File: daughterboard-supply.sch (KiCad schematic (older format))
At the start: 9 parts

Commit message: Remove power diodes
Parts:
- removed D?: PMEG3005EH, Diode_SMD:D_SOD-123F, symbol Diode:PMEG3005EH
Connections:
- wire segments 25 -> 24
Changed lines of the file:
@@
 VCC12V0
 $Comp
-L Diode:PMEG3005EH D?
-U 1 1 6251677E
-P 2000 1550
-AR Path="/62220F27/6251677E" Ref="D?"  Part="1"
-AR Path="/623923F9/6251677E" Ref="D?"  Part="1"
-F 0 "D?" H 2000 1450 50  0000 C CNN
-F 1 "PMEG3005EH" H 2000 1650 50  0000 C CNN
-F 2 "Diode_SMD:D_SOD-123F" H 2000 1375 50  0001 C CNN
-F 3 "https://assets.nexperia.com/documents/data-sheet/PMEGXX05EH_EJ_SER.pdf" H 2000 1550 50  0001 C CNN
-	1    2000 1550
-	-1   0    0    1
-$EndComp
-$Comp
 L antmicroDCDCConverters:AP62301WU-7 U?
 U 1 1 6251678C
@@
 Connection ~ 2350 1550
 Wire Wire Line
-	1650 1550 1850 1550
-Wire Wire Line
 	5900 1550 5500 1550
 Connection ~ 5500 1550
-Wire Wire Line
-	2150 1550 2350 1550
 $Comp
 L antmicroCapacitors0603:C_10u_16V_0603 C?
@@
 EndData
 $EndBitmap
+Wire Wire Line
+	1650 1550 2350 1550
 $EndSCHEMATC

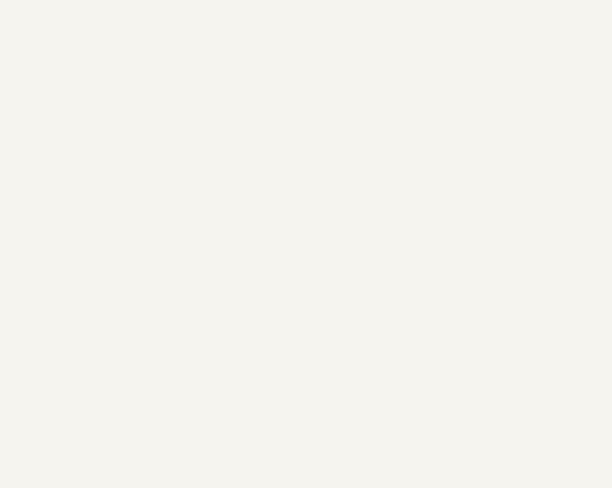
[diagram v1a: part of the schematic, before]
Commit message: Added power distribution connectors
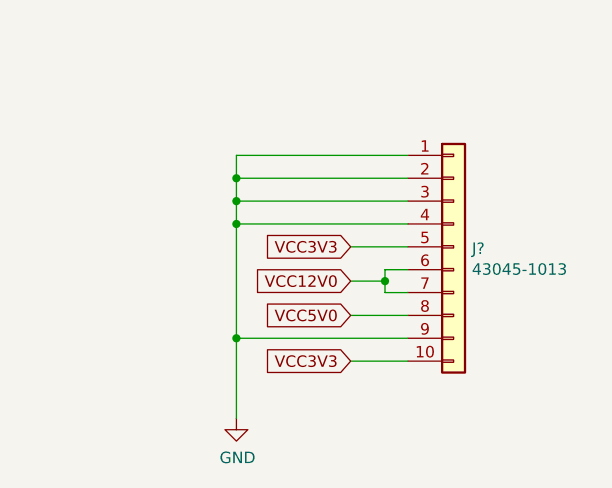
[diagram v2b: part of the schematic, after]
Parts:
- added J?: 43045-1013, antmicro-footprints:43045-1013, symbol antmicroRectangularConnectorsHeadersMalePins:43045-1013
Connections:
- net GND: now also J?.1 (Pin_1), J?.2 (Pin_2), J?.3 (Pin_3), J?.4 (Pin_4), J?.9 (Pin_9)
- net VCC12V0: now also J?.6 (Pin_6), J?.7 (Pin_7)
- net VCC5V0: now also J?.8 (Pin_8)
- new net VCC3V3: J?.10 (Pin_10), J?.5 (Pin_5)
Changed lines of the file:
@@
 Wire Wire Line
 	1650 1550 2350 1550
+$Comp
+L antmicroRectangularConnectorsHeadersMalePins:43045-1013 J?
+U 1 1 62388DA3
+P 9650 1750
+F 0 "J?" H 9730 1792 50  0000 L CNN
+F 1 "43045-1013" H 9730 1701 50  0000 L CNN
+F 2 "antmicro-footprints:43045-1013" H 9650 950 50  0001 C CNN
+F 3 "https://www.molex.com/pdm_docs/sd/430451013_sd.pdf" H 9650 2100 50  0001 C CNN
+F 4 "Molex" H 9650 1050 50  0001 C CNN "Manufacturer"
+F 5 "43045-1013" H 9650 1150 50  0001 C CNN "MPN"
+	1    9650 1750
+	1    0    0    -1
+$EndComp
+$Comp
+L power:GND #PWR?
+U 1 1 62389B5C
+P 8700 2450
+AR Path="/62220F27/62389B5C" Ref="#PWR?"  Part="1"
+AR Path="/623923F9/62389B5C" Ref="#PWR?"  Part="1"
+F 0 "#PWR?" H 8700 2200 50  0001 C CNN
+F 1 "GND" H 8705 2277 50  0000 C CNN
+F 2 "" H 8700 2450 50  0001 C CNN
+F 3 "" H 8700 2450 50  0001 C CNN
+	1    8700 2450
+	1    0    0    -1
+$EndComp
+Wire Wire Line
+	9450 1600 8700 1600
+Wire Wire Line
+	8700 1600 8700 2100
+Wire Wire Line
+	9450 1500 8700 1500
+Wire Wire Line
+	8700 1500 8700 1600
+Connection ~ 8700 1600
+Wire Wire Line
+	9450 1400 8700 1400
+Connection ~ 8700 1500
+Wire Wire Line
+	9450 1300 8700 1300
+Wire Wire Line
+	8700 1300 8700 1400
+Connection ~ 8700 1400
+Wire Wire Line
+	8700 1400 8700 1500
+Wire Wire Line
+	9450 2100 8700 2100
+Connection ~ 8700 2100
+Wire Wire Line
+	8700 2100 8700 2450
+Text GLabel 9200 2000 0    50   Input ~ 0
+VCC5V0
+Text GLabel 9200 1850 0    50   Input ~ 0
+VCC12V0
+Wire Wire Line
+	9200 1850 9350 1850
+Wire Wire Line
+	9350 1850 9350 1800
+Wire Wire Line
+	9350 1800 9450 1800
+Wire Wire Line
+	9450 1900 9350 1900
+Wire Wire Line
+	9350 1900 9350 1850
+Connection ~ 9350 1850
+Wire Wire Line
+	9200 2000 9450 2000
+Text GLabel 9200 1700 0    50   Input ~ 0
+VCC3V3
+Text GLabel 9200 2200 0    50   Input ~ 0
+VCC3V3
+Wire Wire Line
+	9200 2200 9450 2200
+Wire Wire Line
+	9200 1700 9450 1700
 $EndSCHEMATC

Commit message: Schematic complete
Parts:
- gave numbers to parts that had none: 9
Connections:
- no-connect marks 0 -> 1
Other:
- moved on the sheet: C24, C25, C26, C27, J4, L2, R34, R35, U15

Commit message: Loclib update
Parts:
- C24: footprint antmicro-footprints:0603-cap -> nuc-compute-cluster-power-breakout-footprints:0603-cap; symbol antmicroCapacitors0603:C_10u_16V_0603 -> nuc-compute-cluster-power-breakout:C_10u_16V_0603
- C25: footprint antmicro-footprints:0402-cap -> nuc-compute-cluster-power-breakout-footprints:0402-cap; symbol antmicroCapacitors0402:C_100n_0402 -> nuc-compute-cluster-power-breakout:C_100n_0402
- C26, C27: footprint antmicro-footprints:0603-cap -> nuc-compute-cluster-power-breakout-footprints:0603-cap; symbol antmicroCapacitors0603:C_22u_0603 -> nuc-compute-cluster-power-breakout:C_22u_0603
- J4: footprint antmicro-footprints:43045-1013 -> nuc-compute-cluster-power-breakout-footprints:43045-1013; symbol antmicroRectangularConnectorsHeadersMalePins:43045-1013 -> nuc-compute-cluster-power-breakout:43045-1013
- L2: footprint antmicro-footprints:WE_74437336033 -> nuc-compute-cluster-power-breakout-footprints:WE_74437336033; symbol antmicroFixedInductors:74437336033 -> nuc-compute-cluster-power-breakout:74437336033
- R34: footprint antmicro-footprints:0402-res -> nuc-compute-cluster-power-breakout-footprints:0402-res; symbol antmicroResistors0402:R_52k3_0402 -> nuc-compute-cluster-power-breakout:R_52k3_0402
- R35: footprint antmicro-footprints:0402-res -> nuc-compute-cluster-power-breakout-footprints:0402-res; symbol antmicroResistors0402:R_10k_0402 -> nuc-compute-cluster-power-breakout:R_10k_0402
- U15: footprint antmicro-footprints:TSOT23-6 -> nuc-compute-cluster-power-breakout-footprints:TSOT23-6; symbol antmicroDCDCConverters:AP62301WU-7 -> nuc-compute-cluster-power-breakout:AP62301WU-7
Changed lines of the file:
@@
 VCC12V0
 $Comp
-L antmicroDCDCConverters:AP62301WU-7 U?
+L nuc-compute-cluster-power-breakout:AP62301WU-7 U?
 U 1 1 6251678C
 P 3300 2000
@@
 F 0 "U15" H 3300 2465 50  0000 C CNN
 F 1 "AP62301WU-7" H 3300 2374 50  0000 C CNN
-F 2 "antmicro-footprints:TSOT23-6" H 3250 1350 50  0001 C CNN
+F 2 "nuc-compute-cluster-power-breakout-footprints:TSOT23-6" H 3250 1350 50  0001 C CNN
 F 3 "https://www.diodes.com/assets/Datasheets/AP62300_AP62301_AP62300T.pdf" H 3250 1650 50  0001 C CNN
 F 4 "AP62301WU-7" H 3250 1450 50  0001 C CNN "MPN"
@@
 $EndComp
 $Comp
-L antmicroFixedInductors:74437336033 L?
+L nuc-compute-cluster-power-breakout:74437336033 L?
 U 1 1 62516797
 P 4450 1800
@@
 F 0 "L2" H 4450 2105 60  0000 C CNN
 F 1 "74437336033" H 4450 1999 60  0000 C CNN
-F 2 "antmicro-footprints:WE_74437336033" H 5275 2150 60  0001 C CNN
+F 2 "nuc-compute-cluster-power-breakout-footprints:WE_74437336033" H 5275 2150 60  0001 C CNN
 F 3 "https://www.we-online.com/catalog/datasheet/74437336033.pdf" H 4505 1830 60  0001 C CNN
 F 4 "Wurth Elektronik" H 4750 2600 50  0001 C CNN "Manufacturer"
@@
 $EndComp
 $Comp
-L antmicroCapacitors0402:C_100n_0402 C?
+L nuc-compute-cluster-power-breakout:C_100n_0402 C?
 U 1 1 625167A0
 P 3950 2000
@@
 F 0 "C25" V 3850 2150 60  0000 C CNN
 F 1 "C_100n_0402" H 3950 1850 60  0001 C CNN
-F 2 "antmicro-footprints:0402-cap" H 4150 2200 60  0001 L CNN
+F 2 "nuc-compute-cluster-power-breakout-footprints:0402-cap" H 4150 2200 60  0001 L CNN
 F 3 "" H 3950 2000 50  0001 C CNN
 F 4 "Murata" H 4150 2400 60  0001 L CNN "Manufacturer"
@@
 	3700 2200 4700 2200
 $Comp
-L power:GND #PWR?
+L nuc-compute-cluster-power-breakout:GND #PWR?
 U 1 1 625167B6
 P 4700 2650
@@
 	4700 2650 4700 2550
 $Comp
-L power:GND #PWR?
+L nuc-compute-cluster-power-breakout:GND #PWR?
 U 1 1 625167CB
 P 2700 2650
@@
 	2700 2200 2900 2200
 $Comp
-L antmicroCapacitors0603:C_22u_0603 C?
+L nuc-compute-cluster-power-breakout:C_22u_0603 C?
 U 1 1 625167DF
 P 5150 2200
@@
 F 0 "C26" H 5265 2245 60  0000 L CNN
 F 1 "C_22u_0603" H 5150 2050 60  0001 C CNN
-F 2 "antmicro-footprints:0603-cap" H 5350 2400 60  0001 L CNN
+F 2 "nuc-compute-cluster-power-breakout-footprints:0603-cap" H 5350 2400 60  0001 L CNN
 F 3 "" H 5150 2200 50  0001 C CNN
 F 4 "MURATA" H 5350 2600 60  0001 L CNN "Manufacturer"
@@
 $EndComp
 $Comp
-L antmicroCapacitors0603:C_22u_0603 C?
+L nuc-compute-cluster-power-breakout:C_22u_0603 C?
 U 1 1 625167E8
 P 5500 2200
@@
 F 0 "C27" H 5615 2245 60  0000 L CNN
 F 1 "C_22u_0603" H 5500 2050 60  0001 C CNN
-F 2 "antmicro-footprints:0603-cap" H 5700 2400 60  0001 L CNN
+F 2 "nuc-compute-cluster-power-breakout-footprints:0603-cap" H 5700 2400 60  0001 L CNN
 F 3 "" H 5500 2200 50  0001 C CNN
 F 4 "MURATA" H 5700 2600 60  0001 L CNN "Manufacturer"
@@
 	2350 1800 2900 1800
 $Comp
-L power:GND #PWR?
+L nuc-compute-cluster-power-breakout:GND #PWR?
 U 1 1 625167F0
 P 2350 2650
@@
 	5150 1800 5500 1800
 $Comp
-L power:GND #PWR?
+L nuc-compute-cluster-power-breakout:GND #PWR?
 U 1 1 625167FD
 P 5150 2650
@@
 $EndComp
 $Comp
-L power:GND #PWR?
+L nuc-compute-cluster-power-breakout:GND #PWR?
 U 1 1 62516803
 P 5500 2650
@@
 Connection ~ 5500 1800
 $Comp
-L antmicroCapacitors0603:C_10u_16V_0603 C24
+L nuc-compute-cluster-power-breakout:C_10u_16V_0603 C24
 U 1 1 6252106D
 P 2350 2250
 F 0 "C24" H 2150 2350 60  0000 L CNN
 F 1 "C_10u_16V_0603" H 2350 2100 60  0001 C CNN
-F 2 "antmicro-footprints:0603-cap" H 2550 2450 60  0001 L CNN
+F 2 "nuc-compute-cluster-power-breakout-footprints:0603-cap" H 2550 2450 60  0001 L CNN
 F 3 "" H 2350 2250 50  0001 C CNN
 F 4 "MURATA" H 2550 2650 60  0001 L CNN "Manufacturer"
@@
 $EndComp
 $Comp
-L antmicroResistors0402:R_10k_0402 R?
+L nuc-compute-cluster-power-breakout:R_10k_0402 R?
 U 1 1 625167BF
 P 4700 2400
@@
 F 0 "R35" V 4655 2470 60  0000 L CNN
 F 1 "R_10k_0402" H 4700 2250 60  0001 C CNN
-F 2 "antmicro-footprints:0402-res" H 4900 2600 60  0001 L CNN
+F 2 "nuc-compute-cluster-power-breakout-footprints:0402-res" H 4900 2600 60  0001 L CNN
 F 3 "" H 4700 2400 50  0001 C CNN
 F 4 "VISHAY" H 4900 2800 60  0001 L CNN "Manufacturer"
@@
 $EndComp
 $Comp
-L antmicroResistors0402:R_52k3_0402 R34
+L nuc-compute-cluster-power-breakout:R_52k3_0402 R34
 U 1 1 6252687B
 P 4700 2000
 F 0 "R34" V 4655 2070 60  0000 L CNN
 F 1 "R_52k3_0402" H 4700 1850 60  0001 C CNN
-F 2 "antmicro-footprints:0402-res" H 4900 2200 60  0001 L CNN
+F 2 "nuc-compute-cluster-power-breakout-footprints:0402-res" H 4900 2200 60  0001 L CNN
 F 3 "" H 4700 2000 50  0001 C CNN
 F 4 "Panasonic" H 4900 2400 60  0001 L CNN "Manufacturer"
@@
 	1650 1800 2350 1800
 $Comp
-L power:GND #PWR?
+L nuc-compute-cluster-power-breakout:GND #PWR?
 U 1 1 62389B5C
 P 8700 2700
@@
 NoConn ~ 2900 2000
 $Comp
-L antmicroRectangularConnectorsHeadersMalePins:43045-1013 J4
+L nuc-compute-cluster-power-breakout:43045-1013 J4
 U 1 1 62388DA3
 P 9650 2000
 F 0 "J4" H 9730 2042 50  0000 L CNN
 F 1 "43045-1013" H 9730 1951 50  0000 L CNN
-F 2 "antmicro-footprints:43045-1013" H 9650 1200 50  0001 C CNN
+F 2 "nuc-compute-cluster-power-breakout-footprints:43045-1013" H 9650 1200 50  0001 C CNN
 F 3 "https://www.molex.com/pdm_docs/sd/430451013_sd.pdf" H 9650 2350 50  0001 C CNN
 F 4 "Molex" H 9650 1300 50  0001 C CNN "Manufacturer"

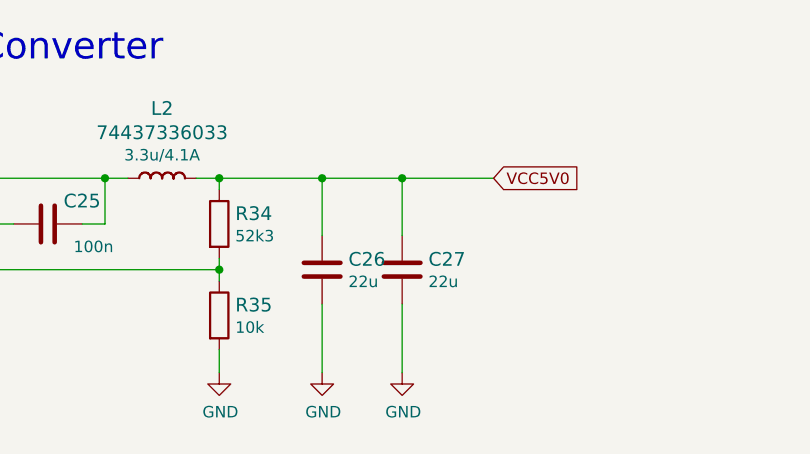
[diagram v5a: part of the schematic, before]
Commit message: Add remarks on the schematic sheets
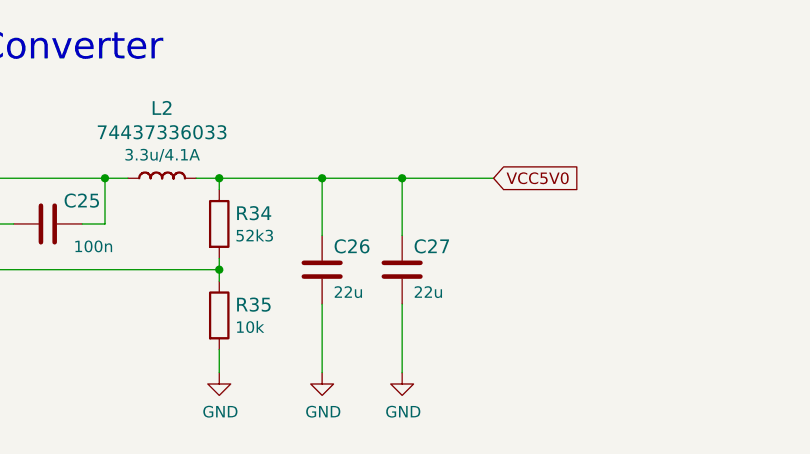
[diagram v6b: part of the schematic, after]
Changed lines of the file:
@@
 AR Path="/62220F27/625167DF" Ref="C?"  Part="1"
 AR Path="/623923F9/625167DF" Ref="C26"  Part="1"
-F 0 "C26" H 5265 2245 60  0000 L CNN
+F 0 "C26" H 5200 2300 60  0000 L CNN
 F 1 "C_22u_0603" H 5150 2050 60  0001 C CNN
 F 2 "nuc-compute-cluster-power-breakout-footprints:0603-cap" H 5350 2400 60  0001 L CNN
@@
 F 4 "MURATA" H 5350 2600 60  0001 L CNN "Manufacturer"
 F 5 "GRM188R60J226MEA0D" H 5350 2500 60  0001 L CNN "MPN"
-F 6 "22u" H 5265 2147 50  0000 L CNN "Val"
+F 6 "22u" H 5200 2100 50  0000 L CNN "Val"
 	1    5150 2200
 	1    0    0    -1
@@
 AR Path="/62220F27/625167E8" Ref="C?"  Part="1"
 AR Path="/623923F9/625167E8" Ref="C27"  Part="1"
-F 0 "C27" H 5615 2245 60  0000 L CNN
+F 0 "C27" H 5550 2300 60  0000 L CNN
 F 1 "C_22u_0603" H 5500 2050 60  0001 C CNN
 F 2 "nuc-compute-cluster-power-breakout-footprints:0603-cap" H 5700 2400 60  0001 L CNN
@@
 F 4 "MURATA" H 5700 2600 60  0001 L CNN "Manufacturer"
 F 5 "GRM188R60J226MEA0D" H 5700 2500 60  0001 L CNN "MPN"
-F 6 "22u" H 5615 2147 50  0000 L CNN "Val"
+F 6 "22u" H 5550 2100 50  0000 L CNN "Val"
 	1    5500 2200
 	1    0    0    -1

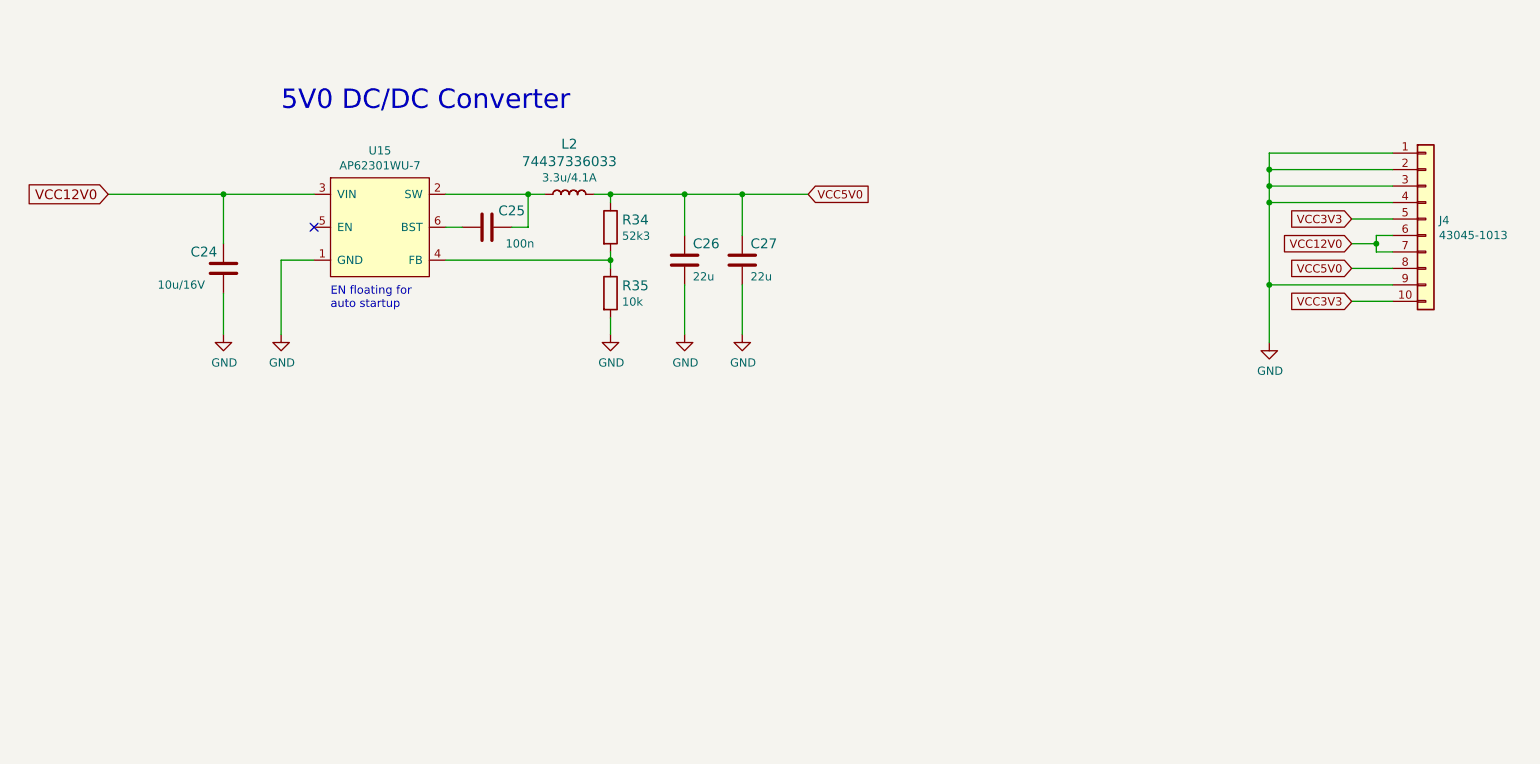
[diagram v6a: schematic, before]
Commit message: Added switch for daughterboard's supply
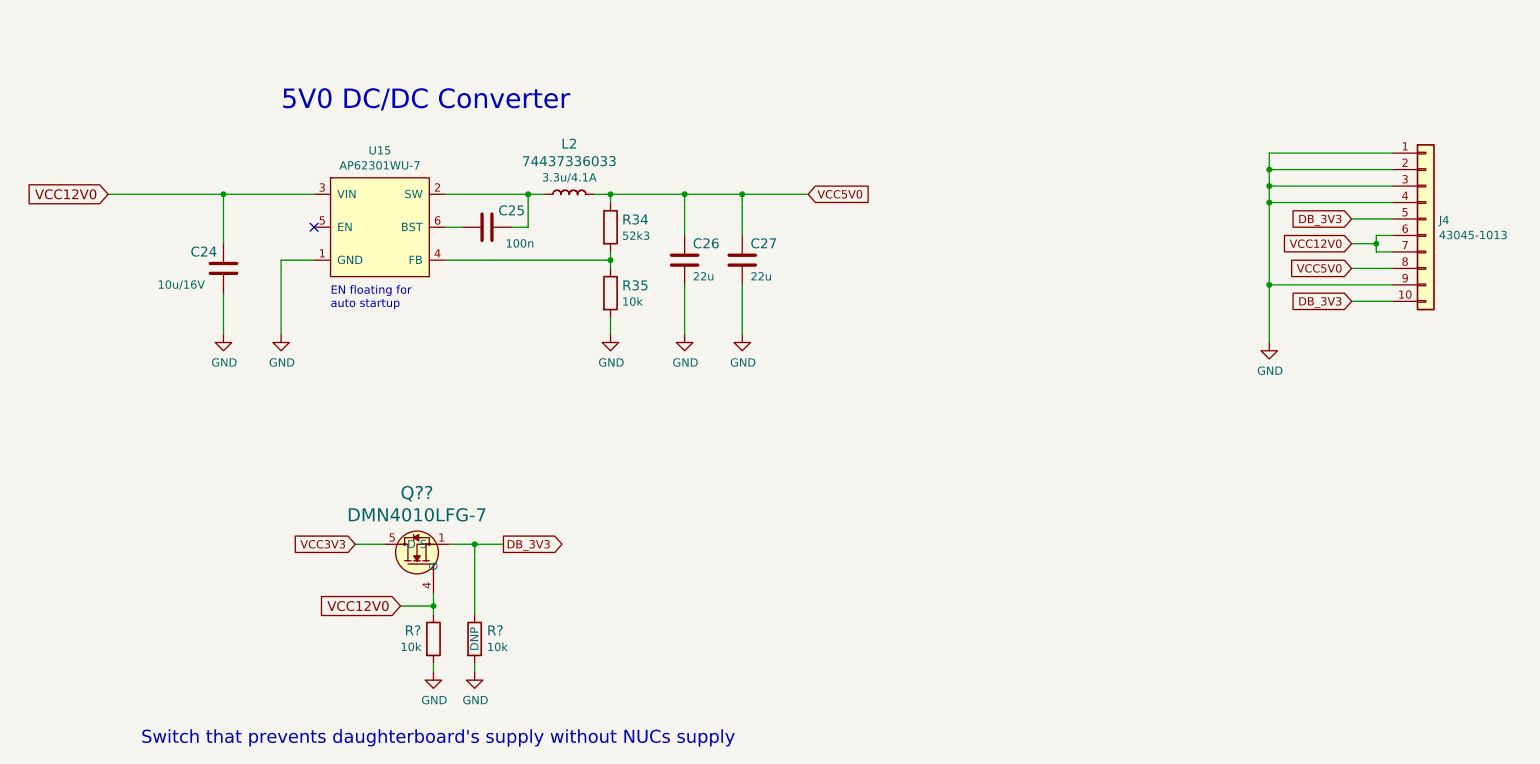
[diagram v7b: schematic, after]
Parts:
- added Q??: DMN4010LFG-7, antmicro-footprints:POWERVDFN-8, symbol antmicroTransistorsFETsMOSFETsSingle:DMN4010LFG-7
- added R? (x2): R_10k_0402, antmicro-footprints:0402-res, symbol antmicroResistors0402:R_10k_0402
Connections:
- net GND: now also R?.2, R?.2
- net VCC12V0: now also Q??.4 (G), R?.1
- net VCC3V3: now also Q??.5 (D), Q??.6 (D), Q??.7 (D), Q??.8 (D); no longer J4.10 (Pin_10), J4.5 (Pin_5)
- new net DB_3V3: J4.10 (Pin_10), J4.5 (Pin_5), Q??.1 (S), Q??.2 (S), Q??.3 (S), R?.1
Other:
- note added: "Switch that prevents daughterboard's supply without NUCs supply"
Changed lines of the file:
@@
 	9200 2250 9450 2250
 Text GLabel 9200 1950 0    50   Input ~ 0
-VCC3V3
+DB_3V3
 Wire Wire Line
 	9200 2450 9450 2450
@@
 $EndComp
 Text GLabel 9200 2450 0    50   Input ~ 0
+DB_3V3
+$Comp
+L antmicroTransistorsFETsMOSFETsSingle:DMN4010LFG-7 Q??
+U 1 1 626C5C42
+P 3525 3950
+F 0 "Q??" V 3861 3950 79  0000 C CNN
+F 1 "DMN4010LFG-7" V 3726 3950 79  0000 C CNN
+F 2 "antmicro-footprints:POWERVDFN-8" H 3525 3950 79  0001 C CNN
+F 3 "https://www.diodes.com/assets/Datasheets/DMN4010LFG.pdf" H 3525 3950 79  0001 C CNN
+F 4 "DMN4010LFG-7" H 3525 3950 79  0001 C CNN "MPN"
+F 5 "Diodes Inc." H 3525 3950 79  0001 C CNN "Manufacturer"
+	1    3525 3950
+	0    -1   -1   0
+$EndComp
+Text GLabel 3150 3925 0    50   Input ~ 0
 VCC3V3
+Wire Wire Line
+	3150 3925 3325 3925
+Text GLabel 4050 3925 2    50   Output ~ 0
+DB_3V3
+Wire Wire Line
+	3725 3925 3875 3925
+Text GLabel 3425 4300 0    59   Input ~ 0
+VCC12V0
+Wire Wire Line
+	3425 4300 3625 4300
+Wire Wire Line
+	3625 4300 3625 4225
+$Comp
+L nuc-compute-cluster-power-breakout:GND #PWR?
+U 1 1 626D67BF
+P 3625 4700
+AR Path="/62220F27/626D67BF" Ref="#PWR?"  Part="1"
+AR Path="/623923F9/626D67BF" Ref="#PWR?"  Part="1"
+F 0 "#PWR?" H 3625 4450 50  0001 C CNN
+F 1 "GND" H 3630 4527 50  0000 C CNN
+F 2 "" H 3625 4700 50  0001 C CNN
+F 3 "" H 3625 4700 50  0001 C CNN
+	1    3625 4700
+	1    0    0    -1
+$EndComp
+$Comp
+L antmicroResistors0402:R_10k_0402 R?
+U 1 1 626D757A
+P 3625 4500
+F 0 "R?" V 3575 4325 60  0000 L CNN
+F 1 "R_10k_0402" H 3625 4350 60  0001 C CNN
+F 2 "antmicro-footprints:0402-res" H 3825 4700 60  0001 L CNN
+F 3 "" H 3625 4500 50  0001 C CNN
+F 4 "VISHAY" H 3825 4900 60  0001 L CNN "Manufacturer"
+F 5 "CRCW040210K0FKEDHP" H 3825 4800 60  0001 L CNN "MPN"
+F 6 "10k" V 3675 4300 50  0000 L CNN "Val"
+	1    3625 4500
+	0    1    1    0
+$EndComp
+Wire Wire Line
+	3625 4700 3625 4650
+Wire Wire Line
+	3625 4350 3625 4300
+Connection ~ 3625 4300
+$Comp
+L nuc-compute-cluster-power-breakout:GND #PWR?
+U 1 1 626DA518
+P 3875 4700
+AR Path="/62220F27/626DA518" Ref="#PWR?"  Part="1"
+AR Path="/623923F9/626DA518" Ref="#PWR?"  Part="1"
+F 0 "#PWR?" H 3875 4450 50  0001 C CNN
+F 1 "GND" H 3880 4527 50  0000 C CNN
+F 2 "" H 3875 4700 50  0001 C CNN
+F 3 "" H 3875 4700 50  0001 C CNN
+	1    3875 4700
+	1    0    0    -1
+$EndComp
+Wire Wire Line
+	3875 4650 3875 4700
+Wire Wire Line
+	3875 4350 3875 3925
+Connection ~ 3875 3925
+Wire Wire Line
+	3875 3925 4050 3925
+$Comp
+L antmicroResistors0402:R_10k_0402 R?
+U 1 1 626D93ED
+P 3875 4500
+F 0 "R?" V 3825 4575 60  0000 L CNN
+F 1 "R_10k_0402" H 3875 4350 60  0001 C CNN
+F 2 "antmicro-footprints:0402-res" H 4075 4700 60  0001 L CNN
+F 3 "" H 3875 4500 50  0001 C CNN
+F 4 "VISHAY" H 4075 4900 60  0001 L CNN "Manufacturer"
+F 5 "CRCW040210K0FKEDHP" H 4075 4800 60  0001 L CNN "MPN"
+F 6 "10k" V 3925 4575 50  0000 L CNN "Val"
+F 7 "DNP" H 3875 4500 50  0000 C CNN "DNP"
+	1    3875 4500
+	0    1    1    0
+$EndComp
+Text Notes 1850 5150 0    79   ~ 0
+Switch that prevents daughterboard's supply without NUCs supply
 $EndSCHEMATC
